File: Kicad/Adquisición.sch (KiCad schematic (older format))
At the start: 28 parts, among them U2 TLC2274, U3 TLC2274

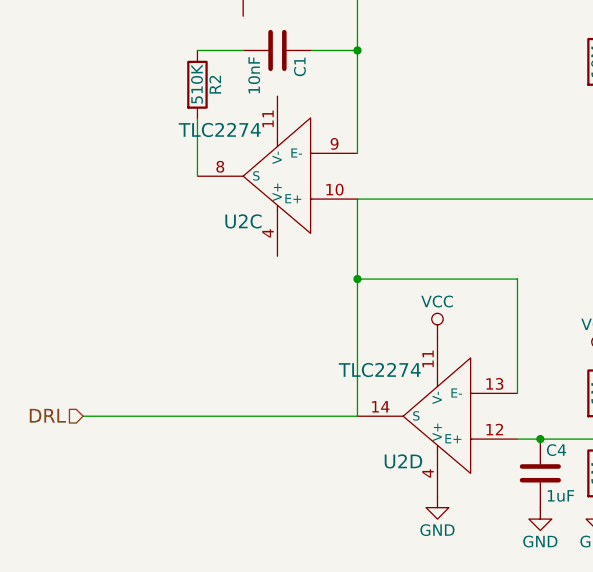
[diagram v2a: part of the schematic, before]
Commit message: Circuito de cargador modificado. A los demás les agregué capacitor en la alimentación, pines sin conexión y cambié BATT- por GND
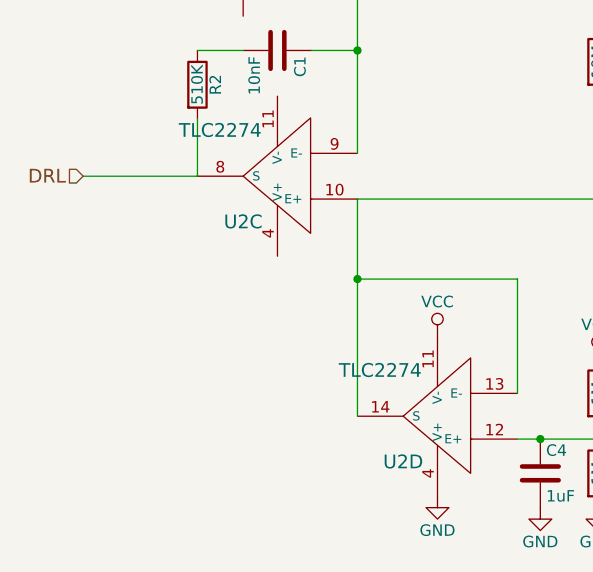
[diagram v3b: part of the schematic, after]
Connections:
- net DRL: now also R2.2, U2.8 (S); no longer R9.2, U2.10 (E+), U2.13 (E-), U2.14 (S), U3.10 (E+)
- new net: R9.2, U2.10 (E+), U2.13 (E-), U2.14 (S), U3.10 (E+)
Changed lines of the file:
@@
 Text HLabel 3000 3550 0    60   Input ~ 0
 E2
-Text HLabel 3000 5550 0    60   Input ~ 0
+Text HLabel 3000 4500 0    60   Input ~ 0
 DRL
-Wire Wire Line
-	3000 5550 4200 5550
 Wire Wire Line
 	3000 3550 3350 3550
@@
 Vout
 Connection ~ 8050 3250
+Wire Wire Line
+	3000 4500 3500 4500
 $EndSCHEMATC

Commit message: Agregados footprints de C_0805 y R_0805 y asociados a resistencias y capacitores del esquemático
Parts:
- C1, C2, C3, C4, C5, C6: footprint (none) -> EMG:C_0805
- R1, R10, R11, R12, R13, R14, R15, R16, R17, R18, R19, R2, R20, R3, R4, R5, R6, R7, R8, R9: footprint (none) -> EMG:R_0805
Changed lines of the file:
@@
 F 0 "R3" V 3730 2450 50  0000 C CNN
 F 1 "43K" V 3650 2450 50  0000 C CNN
-F 2 "" V 3580 2450 50  0001 C CNN
+F 2 "EMG:R_0805" V 3580 2450 50  0001 C CNN
 F 3 "" H 3650 2450 50  0000 C CNN
 	1    3650 2450
@@
 F 0 "R4" V 3730 2950 50  0000 C CNN
 F 1 "43K" V 3650 2950 50  0000 C CNN
-F 2 "" V 3580 2950 50  0001 C CNN
+F 2 "EMG:R_0805" V 3580 2950 50  0001 C CNN
 F 3 "" H 3650 2950 50  0000 C CNN
 	1    3650 2950
@@
 F 0 "R1" V 3430 2700 50  0000 C CNN
 F 1 "10K" V 3350 2700 50  0000 C CNN
-F 2 "" V 3280 2700 50  0001 C CNN
+F 2 "EMG:R_0805" V 3280 2700 50  0001 C CNN
 F 3 "" H 3350 2700 50  0000 C CNN
 	1    3350 2700
@@
 F 0 "R5" V 4430 2100 50  0000 C CNN
 F 1 "22K" V 4350 2100 50  0000 C CNN
-F 2 "" V 4280 2100 50  0001 C CNN
+F 2 "EMG:R_0805" V 4280 2100 50  0001 C CNN
 F 3 "" H 4350 2100 50  0000 C CNN
 	1    4350 2100
@@
 F 0 "R6" V 4430 3300 50  0000 C CNN
 F 1 "22K" V 4350 3300 50  0000 C CNN
-F 2 "" V 4280 3300 50  0001 C CNN
+F 2 "EMG:R_0805" V 4280 3300 50  0001 C CNN
 F 3 "" H 4350 3300 50  0000 C CNN
 	1    4350 3300
@@
 F 0 "R7" V 5080 2100 50  0000 C CNN
 F 1 "10M" V 5000 2100 50  0000 C CNN
-F 2 "" V 4930 2100 50  0001 C CNN
+F 2 "EMG:R_0805" V 4930 2100 50  0001 C CNN
 F 3 "" H 5000 2100 50  0000 C CNN
 	1    5000 2100
@@
 F 0 "R8" V 5080 3300 50  0000 C CNN
 F 1 "10M" V 5000 3300 50  0000 C CNN
-F 2 "" V 4930 3300 50  0001 C CNN
+F 2 "EMG:R_0805" V 4930 3300 50  0001 C CNN
 F 3 "" H 5000 3300 50  0000 C CNN
 	1    5000 3300
@@
 F 0 "R13" V 5630 2500 50  0000 C CNN
 F 1 "430K" V 5550 2500 50  0000 C CNN
-F 2 "" V 5480 2500 50  0001 C CNN
+F 2 "EMG:R_0805" V 5480 2500 50  0001 C CNN
 F 3 "" H 5550 2500 50  0000 C CNN
 	1    5550 2500
@@
 F 0 "R14" V 5630 2900 50  0000 C CNN
 F 1 "430K" V 5550 2900 50  0000 C CNN
-F 2 "" V 5480 2900 50  0001 C CNN
+F 2 "EMG:R_0805" V 5480 2900 50  0001 C CNN
 F 3 "" H 5550 2900 50  0000 C CNN
 	1    5550 2900
@@
 F 0 "R12" V 5480 2700 50  0000 C CNN
 F 1 "43K" V 5400 2700 50  0000 C CNN
-F 2 "" V 5330 2700 50  0001 C CNN
+F 2 "EMG:R_0805" V 5330 2700 50  0001 C CNN
 F 3 "" H 5400 2700 50  0000 C CNN
 	1    5400 2700
@@
 F 0 "C2" H 4675 2050 50  0000 L CNN
 F 1 "0.33uF" H 4675 1850 50  0000 L CNN
-F 2 "" H 4688 1800 50  0001 C CNN
+F 2 "EMG:C_0805" H 4688 1800 50  0001 C CNN
 F 3 "" H 4650 1950 50  0000 C CNN
 	1    4650 1950
@@
 F 0 "C3" H 4675 3550 50  0000 L CNN
 F 1 "0.33uF" H 4675 3350 50  0000 L CNN
-F 2 "" H 4688 3300 50  0001 C CNN
+F 2 "EMG:C_0805" H 4688 3300 50  0001 C CNN
 F 3 "" H 4650 3450 50  0000 C CNN
 	1    4650 3450
@@
 F 0 "R15" V 6480 3350 50  0000 C CNN
 F 1 "43K" V 6400 3350 50  0000 C CNN
-F 2 "" V 6330 3350 50  0001 C CNN
+F 2 "EMG:R_0805" V 6330 3350 50  0001 C CNN
 F 3 "" H 6400 3350 50  0000 C CNN
 	1    6400 3350
@@
 F 0 "R16" V 6780 2550 50  0000 C CNN
 F 1 "43K" V 6700 2550 50  0000 C CNN
-F 2 "" V 6630 2550 50  0001 C CNN
+F 2 "EMG:R_0805" V 6630 2550 50  0001 C CNN
 F 3 "" H 6700 2550 50  0000 C CNN
 	1    6700 2550
@@
 F 0 "R18" V 7080 2700 50  0000 C CNN
 F 1 "215K" V 7000 2700 50  0000 C CNN
-F 2 "" V 6930 2700 50  0001 C CNN
+F 2 "EMG:R_0805" V 6930 2700 50  0001 C CNN
 F 3 "" H 7000 2700 50  0000 C CNN
 	1    7000 2700
@@
 F 0 "R17" V 6780 3550 50  0000 C CNN
 F 1 "215K" V 6700 3550 50  0000 C CNN
-F 2 "" V 6630 3550 50  0001 C CNN
+F 2 "EMG:R_0805" V 6630 3550 50  0001 C CNN
 F 3 "" H 6700 3550 50  0000 C CNN
 	1    6700 3550
@@
 F 0 "C5" H 6925 3800 50  0000 L CNN
 F 1 "0.68uF" H 6925 3600 50  0000 L CNN
-F 2 "" H 6938 3550 50  0001 C CNN
+F 2 "EMG:C_0805" H 6938 3550 50  0001 C CNN
 F 3 "" H 6900 3700 50  0000 C CNN
 	1    6900 3700
@@
 F 0 "R19" V 7330 3700 50  0000 C CNN
 F 1 "10M" V 7250 3700 50  0000 C CNN
-F 2 "" V 7180 3700 50  0001 C CNN
+F 2 "EMG:R_0805" V 7180 3700 50  0001 C CNN
 F 3 "" H 7250 3700 50  0000 C CNN
 	1    7250 3700
@@
 F 0 "R9" V 5330 4000 50  0000 C CNN
 F 1 "10M" V 5250 4000 50  0000 C CNN
-F 2 "" V 5180 4000 50  0001 C CNN
+F 2 "EMG:R_0805" V 5180 4000 50  0001 C CNN
 F 3 "" H 5250 4000 50  0000 C CNN
 	1    5250 4000
@@
 F 0 "C1" H 3875 4050 50  0000 L CNN
 F 1 "10nF" H 3875 3850 50  0000 L CNN
-F 2 "" H 3888 3800 50  0001 C CNN
+F 2 "EMG:C_0805" H 3888 3800 50  0001 C CNN
 F 3 "" H 3850 3950 50  0000 C CNN
 	1    3850 3950
@@
 F 0 "R2" V 3580 4100 50  0000 C CNN
 F 1 "510K" V 3500 4100 50  0000 C CNN
-F 2 "" V 3430 4100 50  0001 C CNN
+F 2 "EMG:R_0805" V 3430 4100 50  0001 C CNN
 F 3 "" H 3500 4100 50  0000 C CNN
 	1    3500 4100
@@
 F 0 "C4" H 5025 5900 50  0000 L CNN
 F 1 "1uF" H 5025 5700 50  0000 L CNN
-F 2 "" H 5038 5650 50  0001 C CNN
+F 2 "EMG:C_0805" H 5038 5650 50  0001 C CNN
 F 3 "" H 5000 5800 50  0000 C CNN
 	1    5000 5800
@@
 F 0 "R11" V 5330 5800 50  0000 C CNN
 F 1 "1M" V 5250 5800 50  0000 C CNN
-F 2 "" V 5180 5800 50  0001 C CNN
+F 2 "EMG:R_0805" V 5180 5800 50  0001 C CNN
 F 3 "" H 5250 5800 50  0000 C CNN
 	1    5250 5800
@@
 F 0 "R10" V 5330 5450 50  0000 C CNN
 F 1 "1M" V 5250 5450 50  0000 C CNN
-F 2 "" V 5180 5450 50  0001 C CNN
+F 2 "EMG:R_0805" V 5180 5450 50  0001 C CNN
 F 3 "" H 5250 5450 50  0000 C CNN
 	1    5250 5450
@@
 F 0 "R20" V 7830 3250 50  0000 C CNN
 F 1 "1600K" V 7750 3250 50  0000 C CNN
-F 2 "" V 7680 3250 50  0001 C CNN
+F 2 "EMG:R_0805" V 7680 3250 50  0001 C CNN
 F 3 "" H 7750 3250 50  0000 C CNN
 	1    7750 3250
@@
 F 0 "C6" H 8075 3500 50  0000 L CNN
 F 1 "1uF" H 8075 3300 50  0000 L CNN
-F 2 "" H 8088 3250 50  0001 C CNN
+F 2 "EMG:C_0805" H 8088 3250 50  0001 C CNN
 F 3 "" H 8050 3400 50  0000 C CNN
 	1    8050 3400

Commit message: Asociado footprint de msp430
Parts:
- U2, U3: footprint (none) -> EMG:TSSOP-14_4.4x5mm_Pitch0.65mm
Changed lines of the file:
@@
 F 0 "U2" H 3850 2150 60  0000 C CNN
 F 1 "TLC2274" H 3950 1750 60  0000 C CNN
-F 2 "" H 3700 1950 60  0001 C CNN
+F 2 "EMG:TSSOP-14_4.4x5mm_Pitch0.65mm" H 3700 1950 60  0001 C CNN
 F 3 "" H 3700 1950 60  0000 C CNN
 	1    3700 1950
@@
 F 0 "U2" H 3850 3650 60  0000 C CNN
 F 1 "TLC2274" H 3950 3250 60  0000 C CNN
-F 2 "" H 3700 3450 60  0001 C CNN
+F 2 "EMG:TSSOP-14_4.4x5mm_Pitch0.65mm" H 3700 3450 60  0001 C CNN
 F 3 "" H 3700 3450 60  0000 C CNN
 	2    3700 3450
@@
 F 0 "U3" H 5900 2250 60  0000 C CNN
 F 1 "TLC2274" H 6000 1850 60  0000 C CNN
-F 2 "" H 5750 2050 60  0001 C CNN
+F 2 "EMG:TSSOP-14_4.4x5mm_Pitch0.65mm" H 5750 2050 60  0001 C CNN
 F 3 "" H 5750 2050 60  0000 C CNN
 	1    5750 2050
@@
 F 0 "U3" H 5900 3550 60  0000 C CNN
 F 1 "TLC2274" H 6000 3150 60  0000 C CNN
-F 2 "" H 5750 3350 60  0001 C CNN
+F 2 "EMG:TSSOP-14_4.4x5mm_Pitch0.65mm" H 5750 3350 60  0001 C CNN
 F 3 "" H 5750 3350 60  0000 C CNN
 	2    5750 3350
@@
 F 0 "U3" H 7200 3450 60  0000 C CNN
 F 1 "TLC2274" H 7300 3050 60  0000 C CNN
-F 2 "" H 7050 3250 60  0001 C CNN
+F 2 "EMG:TSSOP-14_4.4x5mm_Pitch0.65mm" H 7050 3250 60  0001 C CNN
 F 3 "" H 7050 3250 60  0000 C CNN
 	4    7050 3250
@@
 F 0 "U3" H 6850 4400 60  0000 C CNN
 F 1 "TLC2274" H 6950 4000 60  0000 C CNN
-F 2 "" H 6700 4200 60  0001 C CNN
+F 2 "EMG:TSSOP-14_4.4x5mm_Pitch0.65mm" H 6700 4200 60  0001 C CNN
 F 3 "" H 6700 4200 60  0000 C CNN
 	3    6700 4200
@@
 F 0 "U2" H 4000 4700 60  0000 C CNN
 F 1 "TLC2274" H 4100 4300 60  0000 C CNN
-F 2 "" H 3850 4500 60  0001 C CNN
+F 2 "EMG:TSSOP-14_4.4x5mm_Pitch0.65mm" H 3850 4500 60  0001 C CNN
 F 3 "" H 3850 4500 60  0000 C CNN
 	3    3850 4500
@@
 F 0 "U2" H 4700 5750 60  0000 C CNN
 F 1 "TLC2274" H 4800 5350 60  0000 C CNN
-F 2 "" H 4550 5550 60  0001 C CNN
+F 2 "EMG:TSSOP-14_4.4x5mm_Pitch0.65mm" H 4550 5550 60  0001 C CNN
 F 3 "" H 4550 5550 60  0000 C CNN
 	4    4550 5550

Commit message: Agregado jumpers para programar el micro
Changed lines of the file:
@@
 	7050 4600 7050 4300
 Wire Wire Line
-	4200 4400 4200 2700
+	4200 2700 4200 4400
 Wire Wire Line
 	4200 2700 4350 2700
@@
 	5750 2800 5750 3000
 Wire Wire Line
-	4200 5550 4200 4600
+	4200 4600 4200 5550
 Wire Wire Line
 	4900 5450 4900 4950
